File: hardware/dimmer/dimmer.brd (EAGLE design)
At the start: 99.7 x 40.6 mm, 38 parts, among them IC1 MEGA328PU, IC2 RFM12, IC3 7812L, IC4 LP2950Z, K1 G6D-1A-ASI12VDC, T1 BC547, T2 BC547, X1 AC In, X2 DIM Out, X3 AC Out

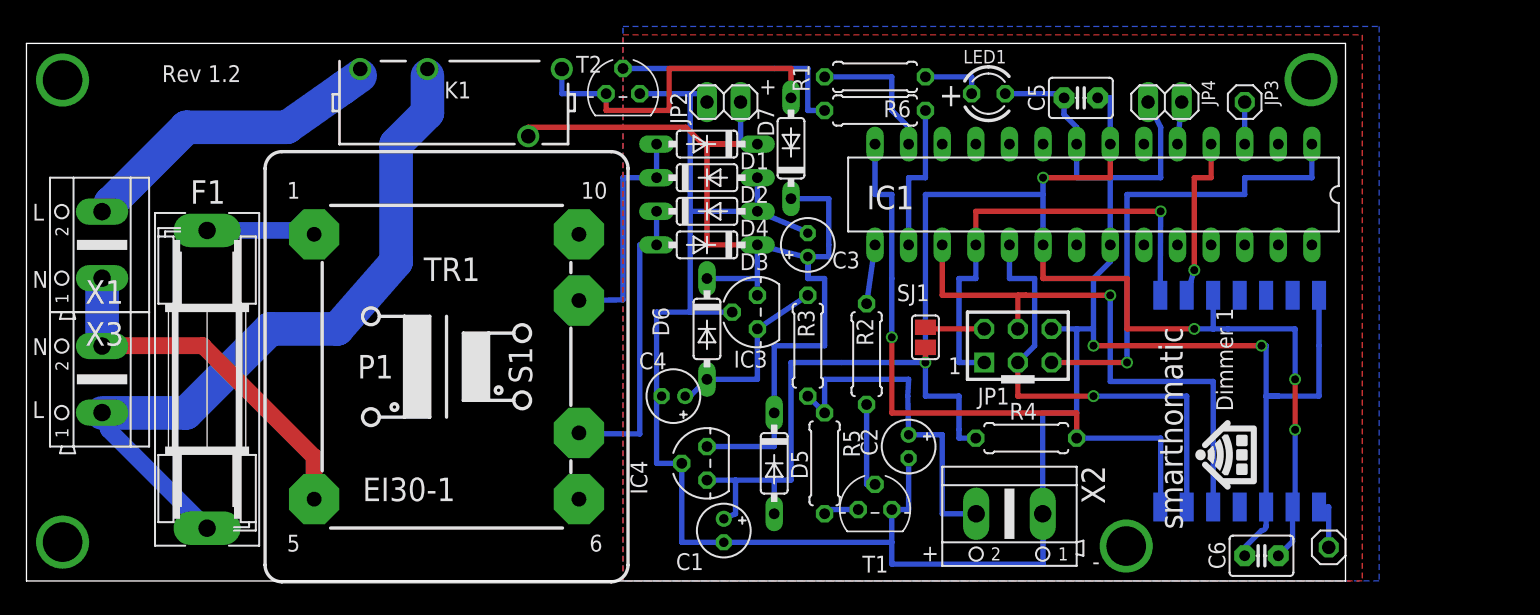
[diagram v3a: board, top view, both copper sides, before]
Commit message: Updated dimmer hardware to V1.3, where RFM12 power is connected to an ATMega I/O pin to restart it if necessary using the transceiver watchdog functionality.
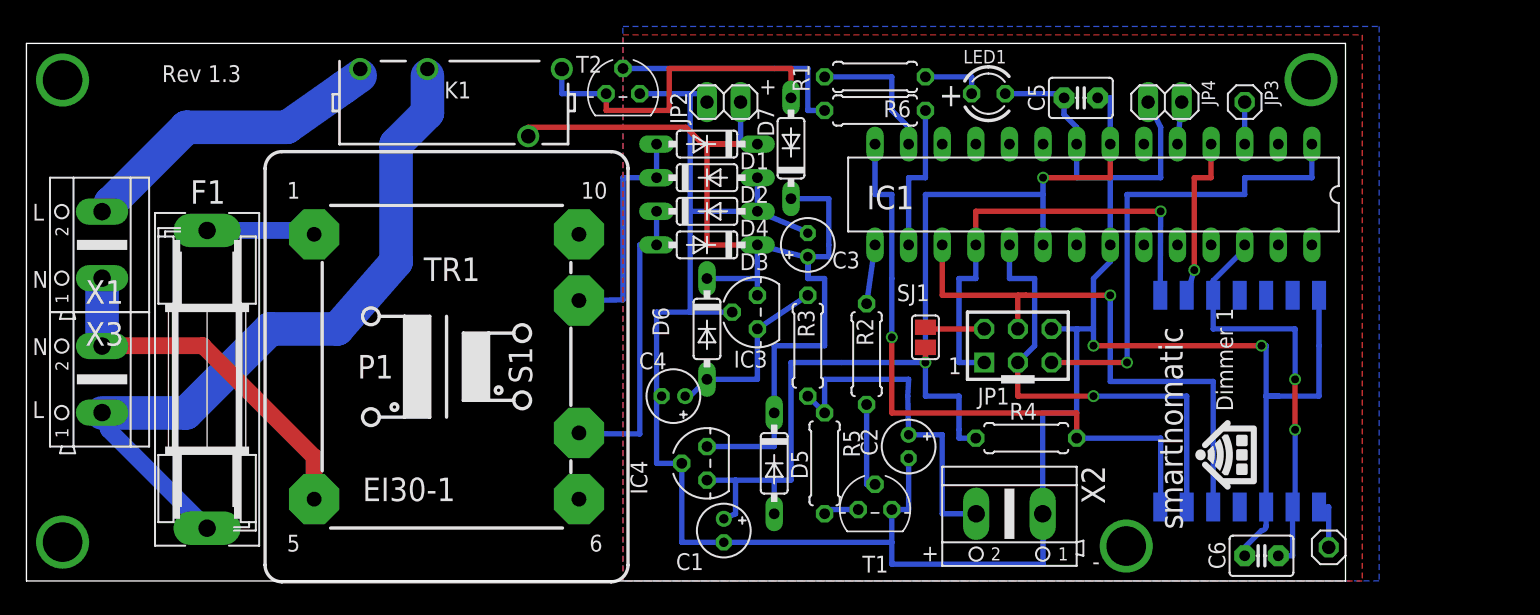
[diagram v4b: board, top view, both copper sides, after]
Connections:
- new net N$28: C6.1, IC1.26, IC2.3, IC2.9
- net VCC: no longer C6.1, IC2.3, IC2.9
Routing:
- net VCC: track 126.7 -> 80.9 mm, vias 5 -> 2
- net N$28: track 0.00 -> 32.1 mm, vias 0 -> 2
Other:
- board text added: "Rev 1.3"
- board text removed: "Rev 1.2"
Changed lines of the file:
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@@
 <?xml version="1.0" encoding="utf-8"?>
 <!DOCTYPE eagle SYSTEM "eagle.dtd">
-<eagle version="6.4">
+<eagle version="7.3.0">
 <drawing>
 <settings>
@@
 <text x="81.68021875" y="3.898665625" size="1.778" layer="25" font="vector" rot="R90">smarthomatic</text>
 <text x="85.476909375" y="12.837490625" size="1.27" layer="25" font="vector" rot="R90">Dimmer 1</text>
-<text x="4.5279" y="37.7094375" size="1.27" layer="25">Rev 1.2</text>
+<text x="4.5279" y="37.7094375" size="1.27" layer="25">Rev 1.3</text>
 <text x="65.0875" y="35.8775" size="1.778" layer="25" rot="MR0">+</text>
 <rectangle x1="87.237196875" y1="7.536375" x2="87.318196875" y2="7.54215625" layer="25" rot="R90"/>
@@
 <pass name="Default">
 <param name="RoutingGrid" value="50mil"/>
+<param name="AutoGrid" value="1"/>
+<param name="Efforts" value="0"/>
+<param name="TopRouterVariant" value="1"/>
 <param name="tpViaShape" value="round"/>
 <param name="PrefDir.1" value="|"/>
@@
 </signal>
 <signal name="VCC">
-<contactref element="IC2" pad="3"/>
 <contactref element="R4" pad="1"/>
-<contactref element="IC2" pad="9"/>
 <contactref element="IC4" pad="1"/>
 <contactref element="C1" pad="+"/>
@@
 <wire x1="47.879" y1="5.08" x2="47.879" y2="7.62" width="0.4064" layer="16"/>
 <wire x1="47.879" y1="7.62" x2="45.72" y2="7.62" width="0.4064" layer="16"/>
-<wire x1="90.17" y1="5.4" x2="89.98" y2="5.59" width="0.4064" layer="16"/>
 <wire x1="55.88" y1="16.51" x2="52.07" y2="16.51" width="0.4064" layer="16"/>
 <wire x1="52.07" y1="16.51" x2="52.07" y2="7.62" width="0.4064" layer="16"/>
@@
 <wire x1="50.8" y1="5.08" x2="50.8" y2="7.62" width="0.4064" layer="16"/>
 <contactref element="C5" pad="1"/>
-<contactref element="C6" pad="1"/>
 <wire x1="55.88" y1="16.51" x2="62.23" y2="16.51" width="0.4064" layer="16"/>
 <wire x1="62.23" y1="16.51" x2="62.23" y2="13.97" width="0.4064" layer="16"/>
@@
 <wire x1="64.77" y1="11.43" x2="64.77" y2="10.795" width="0.4064" layer="16"/>
 <wire x1="64.77" y1="10.795" x2="66.04" y2="10.795" width="0.4064" layer="16"/>
-<wire x1="88.9" y1="1.905" x2="89.98" y2="2.985" width="0.4064" layer="16"/>
-<wire x1="89.98" y1="2.985" x2="89.98" y2="5.59" width="0.4064" layer="16"/>
-<wire x1="89.98" y1="5.59" x2="90.17" y2="5.78" width="0.4064" layer="16"/>
-<wire x1="90.17" y1="5.78" x2="90.17" y2="11.43" width="0.4064" layer="16"/>
-<via x="90.17" y="11.43" extent="1-16" drill="0.6" shape="square"/>
-<wire x1="90.17" y1="11.43" x2="90.17" y2="15.24" width="0.4064" layer="1"/>
-<via x="90.17" y="15.24" extent="1-16" drill="0.6" shape="square"/>
-<wire x1="90.17" y1="15.24" x2="90.17" y2="19.05" width="0.4064" layer="16"/>
-<wire x1="90.17" y1="19.05" x2="85.09" y2="19.05" width="0.4064" layer="16"/>
-<wire x1="85.09" y1="19.05" x2="83.98" y2="19.05" width="0.4064" layer="16"/>
-<wire x1="83.98" y1="19.05" x2="83.98" y2="21.59" width="0.4064" layer="16"/>
-<wire x1="71.12" y1="25.4" x2="71.12" y2="22.86" width="0.4064" layer="1"/>
-<wire x1="71.12" y1="22.86" x2="77.47" y2="22.86" width="0.4064" layer="1"/>
-<wire x1="77.47" y1="22.86" x2="77.47" y2="19.05" width="0.4064" layer="1"/>
-<wire x1="77.47" y1="19.05" x2="82.55" y2="19.05" width="0.4064" layer="1"/>
-<via x="82.55" y="19.05" extent="1-16" drill="0.6" shape="square"/>
-<wire x1="82.55" y1="19.05" x2="83.98" y2="19.05" width="0.4064" layer="16"/>
+<wire x1="90.17" y1="11.43" x2="90.17" y2="11.43" width="0" layer="19" extent="1-16"/>
+<wire x1="90.17" y1="11.43" x2="90.17" y2="15.24" width="0" layer="19" extent="1-16"/>
+<wire x1="90.17" y1="15.24" x2="90.17" y2="15.24" width="0" layer="19" extent="1-16"/>
+<wire x1="90.17" y1="15.24" x2="90.17" y2="19.05" width="0" layer="19" extent="1-16"/>
+<wire x1="90.17" y1="19.05" x2="85.09" y2="19.05" width="0" layer="19" extent="1-16"/>
+<wire x1="85.09" y1="19.05" x2="83.98" y2="19.05" width="0" layer="19" extent="1-16"/>
+<wire x1="71.12" y1="25.4" x2="71.12" y2="22.86" width="0" layer="19" extent="1-16"/>
+<wire x1="71.12" y1="22.86" x2="77.47" y2="22.86" width="0" layer="19" extent="1-16"/>
+<wire x1="77.47" y1="22.86" x2="77.47" y2="19.05" width="0" layer="19" extent="1-16"/>
+<wire x1="77.47" y1="19.05" x2="82.55" y2="19.05" width="0" layer="19" extent="1-16"/>
+<wire x1="82.55" y1="19.05" x2="82.55" y2="19.05" width="0" layer="19" extent="1-16"/>
+<wire x1="82.55" y1="19.05" x2="83.98" y2="19.05" width="0" layer="19" extent="1-16"/>
 <wire x1="76.2" y1="33.02" x2="76.2" y2="30.48" width="0.4064" layer="1"/>
 <wire x1="76.2" y1="30.48" x2="71.12" y2="30.48" width="0.4064" layer="1"/>
@@
 <wire x1="62.23" y1="19.05" x2="62.23" y2="19.177" width="0.4064" layer="1"/>
 </signal>
+<signal name="N$28">
+<contactref element="IC2" pad="9"/>
+<contactref element="C6" pad="1"/>
+<contactref element="IC1" pad="26"/>
+<contactref element="IC2" pad="3"/>
+<wire x1="88.9" y1="1.905" x2="89.98" y2="1.905" width="0.4064" layer="16"/>
+<wire x1="89.98" y1="1.905" x2="89.98" y2="5.59" width="0.4064" layer="16"/>
+<wire x1="89.98" y1="5.59" x2="90.17" y2="5.59" width="0.4064" layer="16"/>
+<wire x1="90.17" y1="5.59" x2="90.17" y2="11.43" width="0.4064" layer="16"/>
+<via x="90.17" y="11.43" extent="1-16" drill="0.6" shape="square"/>
+<wire x1="90.17" y1="11.43" x2="90.17" y2="15.24" width="0.4064" layer="1"/>
+<via x="90.17" y="15.24" extent="1-16" drill="0.6" shape="square"/>
+<wire x1="90.17" y1="15.24" x2="90.17" y2="19.05" width="0.4064" layer="16"/>
+<wire x1="90.17" y1="19.05" x2="83.98" y2="19.05" width="0.4064" layer="16"/>
+<wire x1="83.98" y1="19.05" x2="83.98" y2="21.59" width="0.4064" layer="16"/>
+<wire x1="83.98" y1="21.59" x2="83.98" y2="22.7025" width="0.4064" layer="16"/>
+<wire x1="83.98" y1="22.7025" x2="86.0425" y2="24.765" width="0.4064" layer="16"/>
+<wire x1="86.0425" y1="24.765" x2="86.36" y2="24.765" width="0.4064" layer="16"/>
+<wire x1="86.36" y1="24.765" x2="86.36" y2="25.4" width="0.4064" layer="16"/>
+</signal>
 </signals>
